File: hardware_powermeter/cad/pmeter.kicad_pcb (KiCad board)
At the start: 4 copper layers, 47 x 14 mm, 59 parts, among them J101 conector magnetico 6 vias, J102 furos da celula, J301 furos da ponte, U101 nPM1100-QDAB, U102 MAX17048G+T10, U201 HOLYIOT-26001-A, U301 ADS1220IRVAR, U302 TPS22916BYFPR, U401 BMA400, U402 TMP117AIDRVR

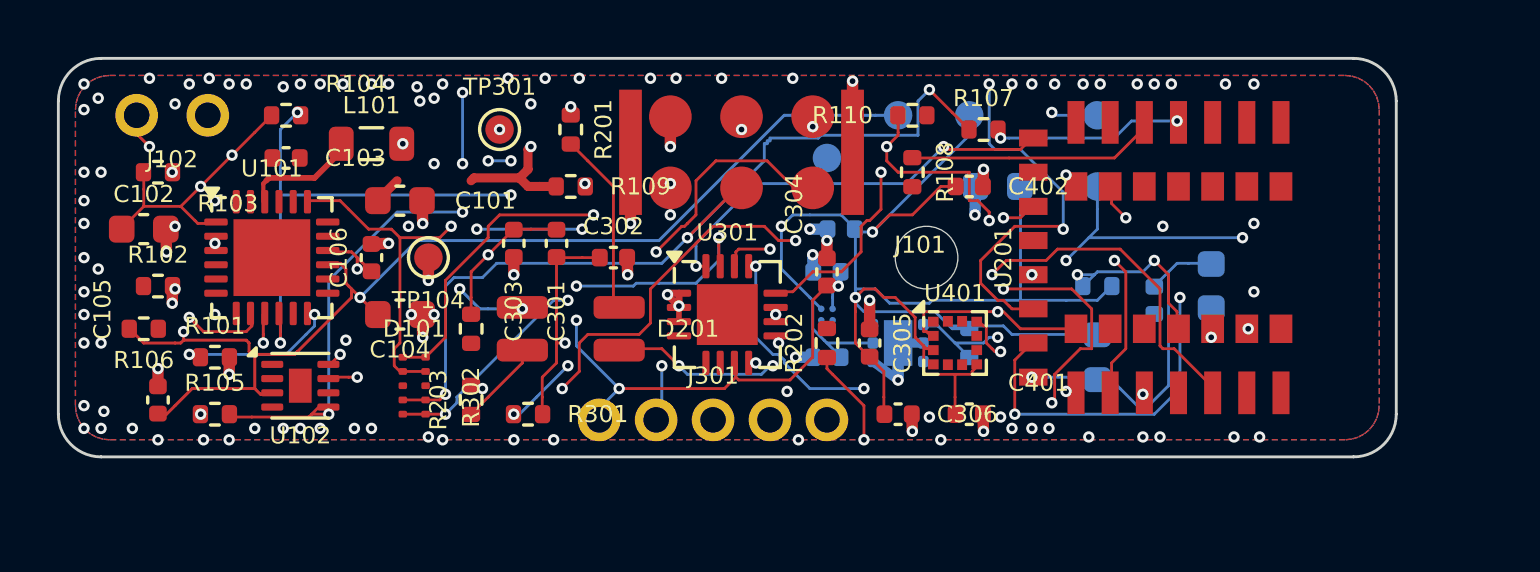
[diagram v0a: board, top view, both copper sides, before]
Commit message: feat(hardware): move the cell beside the board and put every passive on the back
The owner's decision on 2026-09-30, and it changes the board more than it
changes the pod. The cell used to lie against the back over x 1.5 to 26 -
the whole energy block - so the parts that needed relief the most had no
back face at all. Beside the board it takes nothing, the back is free end
to end, and the pod loses the cell from its stack: about 6.5 mm tall
instead of 10.

So the board is 50 x 16 (it grows more across than along, which is the pod
shape that is wanted: low and wide, not long), the back ceiling is 1.5 mm,
and 43 of the 58 parts move to it - every resistor, every capacitor and the
ferrite. Only C104 and C105 stay on the front, because the buck's switching
loop must not cross the board.

The reason is measured, not argued. On the empty grid, before a single
track: F.Cu had 55.2% of its cells free, In2.Cu 87.1% and B.Cu 81.6%.
Nearly half the top layer was pad and clearance, and every routing failure
read "sem caminho ate (x; y) na camada 0". Thinning the track does not fix
that, because the pad does not thin.

What it bought, all from the dry run and the DRC:

  AL1  11 of 19 capacitors out of limit, 3.85 mm average -> 5 of 19, 1.59
  AN1  the analogue corner 3.3 mm from the buck -> 10.9 mm, and 5.9 from
       the module: MET
  AN2  filter parts up to 9.8 mm from their pin -> 3.8 mm at most: MET
  US1  serial over the switching node: MET
  dry run 14 rules met and 6 violated -> 18 met and 2 violated
  routing 93 connections -> 99, and still zero DRC errors

A decoupling capacitor on the back, under the pin it serves, is one via
away - closer than anything that was left free on the front, which is what
AL1 had been asking for all along.

Track and clearance are the fabricator's minimum for four layers (0.0889),
with the router drawing 0.09 and keeping its own clearance at 0.10. That
last number is not cosmetic: at 0.09 the project's own check became LOOSER
than the DRC 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
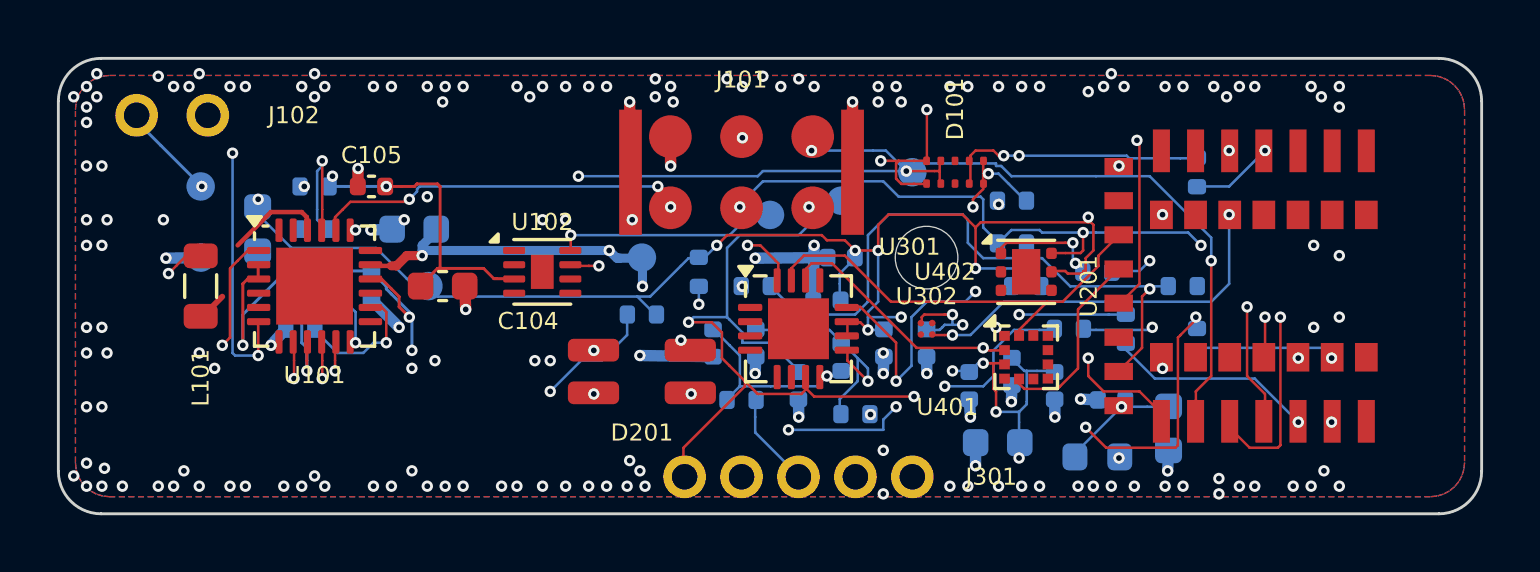
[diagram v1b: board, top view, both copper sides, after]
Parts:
- C101, C102, C103, C106, C301, C302, C303, C304, C305, C306, C401, C402, R101, R102, R103, R104, R105, R106, R107, R108, R109, R110, R201, R202, R203, R301, R302, TP104, TP301: moved to B.Cu
- U302, U402: moved to F.Cu
- moved R105 28.9 mm to (59.0, 33.0)
- moved TP102 24.6 mm to (30.0, 29.5)
- moved R201 23.2 mm to (65.0, 35.0)
- moved R203 23.1 mm to (62.5, 34.5)
- moved D101 20.4 mm to (56.5, 29.0), turned to 90 degrees
- moved TP103 19.9 mm to (38.0, 33.0)
- moved R103 17.7 mm to (45.5, 34.0)
- moved R104 15.5 mm to (47.5, 32.5), turned to 90 degrees
- moved TP301 12.3 mm to (52.5, 30.0)
- moved TP201 11.5 mm to (50.0, 30.5)
- moved R301 11.5 mm to (53.0, 37.5)
- moved R110 11.2 mm to (64.5, 33.0), turned to 180 degrees
- moved C301 10.8 mm to (52.5, 35.5)
- moved C105 10.6 mm to (36.0, 29.5), turned to 180 degrees
- moved R302 9.82 mm to (49.0, 37.0), turned to 0 degrees
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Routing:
- net SHPACT: track 0.00 -> 55.5 mm, vias 0 -> 3
- net GAUGE_ALRT: track 50.8 -> 0.00 mm, vias 6 -> 0
- net VBAT: track 48.2 -> 19.1 mm
- net LED_B: track 35.3 -> 7.34 mm, vias 4 -> 1
- net LED_R: track 31.0 -> 5.07 mm, vias 2 -> 1
- net 3V0: track 109.3 -> 85.1 mm, vias 10 -> 16
- net LED_KG: track 34.2 -> 14.2 mm, vias 5 -> 2
- net LED_KR: track 6.50 -> 26.0 mm, vias 0 -> 3
- net LED_KB: track 3.05 -> 22.2 mm, vias 0 -> 4
- net VBUS_SENSE: track 38.9 -> 22.1 mm, vias 5 -> 1
- net IMU_CS: track 16.6 -> 0.00 mm, vias 2 -> 0
- net EXC_EN: track 0.00 -> 13.6 mm, vias 0 -> 2
- net ERR_N: track 38.3 -> 51.0 mm, vias 4 -> 3
- net UART_RX: track 57.8 -> 46.1 mm, vias 4 -> 5
- net LED_G: track 0.00 -> 11.4 mm, vias 0 -> 2
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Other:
- board size 47 x 14 mm -> 50 x 16 mm
- board text added: "BIKE POWER METER - placa 50 x 16 mm, 0.8 mm, 4 camadas"
- board text removed: "BIKE POWER METER - placa 47 x 14 mm, 0.8 mm, 4 camadas"

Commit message: feat(hardware): the routed board, its drawings and the pod that no longer fits
663 tracks, 172 vias, ZERO DRC errors and 17 connections still open, on the
50 x 16 board with every passive on the back. The seven copper sheets, the
assembly drawing, the 3D views and the pod's STLs were all regenerated from
it.

The pod now FAILS its own PD10 and PD17, and that is correct: it is 21.0 mm
wide against the 20 mm target, because the board grew to 16 mm while the pod
still stacks the cell UNDER it (floor 1.0 + cell 4.0 + air 0.5 + board 0.8 +
ceiling 2.7 + lid 1.0). The decision of 2026-09-30 was to put the cell BESIDE
the board so the device gets lower; the board was rebuilt for it and the pod
was not. The dry run says so out loud instead of hiding it, which is what it
is for.
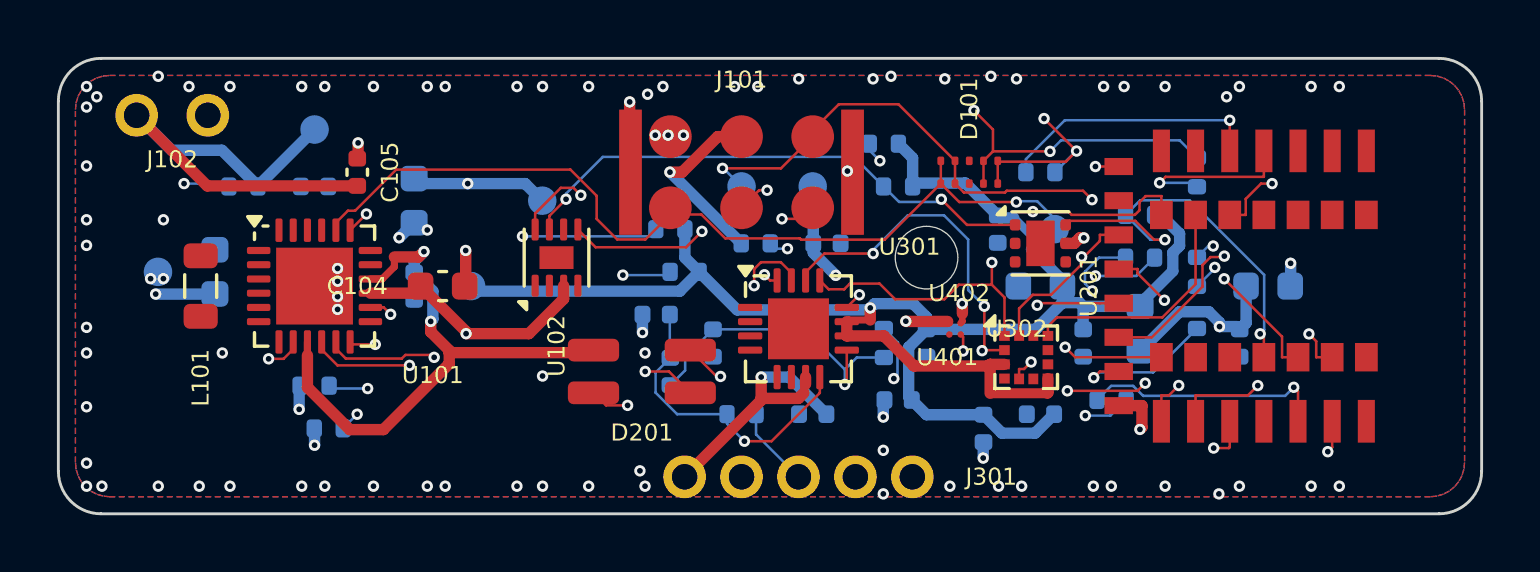
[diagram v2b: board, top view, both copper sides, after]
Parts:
- moved TP201 10.0 mm to (60.0, 31.0)
- moved R205 7.62 mm to (54.5, 29.5)
- moved R105 7.07 mm to (54.0, 28.0)
- moved C202 6.10 mm to (67.5, 33.0), turned to 180 degrees
- moved C301 6.02 mm to (46.5, 36.0), turned to -90 degrees
- moved TP202 6.02 mm to (49.0, 29.5)
- moved C203 5.70 mm to (59.5, 33.0)
- moved C308 5.59 mm to (58.0, 31.0), turned to 90 degrees
- moved C307 4.95 mm to (52.0, 31.5), turned to 180 degrees
- moved C201 4.92 mm to (66.5, 35.0), turned to 90 degrees
- moved FB201 4.74 mm to (63.0, 34.5), turned to 90 degrees
- moved R204 4.61 mm to (63.0, 30.5)
- moved TP102 4.47 mm to (34.0, 27.5)
- moved C305 4.30 mm to (54.5, 37.0)
- moved TP101 4.03 mm to (42.0, 30.0)
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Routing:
- net SHPACT: track 55.5 -> 0.00 mm, vias 3 -> 0
- net GAUGE_ALRT: track 0.00 -> 32.9 mm, vias 0 -> 3
- net VBAT: track 19.1 -> 40.3 mm, vias 3 -> 1
- net I2C_SDA: track 33.4 -> 50.8 mm, vias 4 -> 3
- net SPI_MISO: track 8.14 -> 24.5 mm
- net SHPHLD: track 8.10 -> 22.5 mm
- net EXC_EN: track 13.6 -> 27.7 mm, vias 2 -> 4
- net GND: track 24.9 -> 11.2 mm, vias 165 -> 91
- net 3V0: track 85.1 -> 71.6 mm, vias 16 -> 3
- net VBUS_SENSE: track 22.1 -> 35.5 mm, vias 1 -> 2
- net 3V0_EXC: track 33.5 -> 22.2 mm, vias 4 -> 3
- net SPI_SCK: track 15.6 -> 25.5 mm, vias 0 -> 2
- net ERR_N: track 51.0 -> 41.1 mm
- net LED_G: track 11.4 -> 21.1 mm
- net SWCLK_J: track 9.56 -> 18.3 mm
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
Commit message: feat(hardware): net classes from the current table, and the ground left to its plane
Two changes to what the DSN tells Freerouting, both because the router can
only be as good as what it is told.

The three hand-written net classes lied in both directions. Measured against
the IPC-2221 width that route.largura() computes for each net:

    net         IPC asks   the DSN sent
    3V0            0.090       0.40
    3V0_EXC        0.090       0.40
    3V0_MOD        0.090       0.40
    VBAT           0.105       0.40
    VSYS           0.105       0.40
    BUCK_SW        0.204       0.09

Four times wider than the norm asks spends channel that is needed - 3V0 was
one of the nets that would not close - and BUCK_SW, which carries the
inductor's 350 mA, went at signal width. make_netclasses.py now generates one
class per width, rounded up in steps of 0.01 mm, straight from that table.
AL2 passes with ZERO narrowings as a result.

The USB class is gone with them: the nRF54L15 has no USB, the two contacts
that carried D+ and D- now carry UART, and there is no differential pair on
this board. An unused differential-pair class was what gave Freerouting a
narrower width to fall back on - ten tracks of 0.0674 mm.

And GND leaves the DSN entirely. It is 51 of this board's 159 connections,
32 percent, and every one of them is answered by the pour of its own face
plus a stitching via, which stitch_gnd.py places afterwards. Letting the
router spend a third of its space on what the plane already solves is waste.

What was tried and measured as NOT worth it, so it is not here: a 0.45 mm
escape ring around all seven fine-pitch ICs closed one more connection (16
against 17) and took AL1 from 11 to 12 capacitors out of limit, with C105
15.6 mm from the U102 it decouples - at that distance it decouples nothing.
The ring on U101 alone gave 18, worse than no ring. All three sit inside the
router's own run-to-run variation, so what decides is the number that does
not vary: how far the dec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
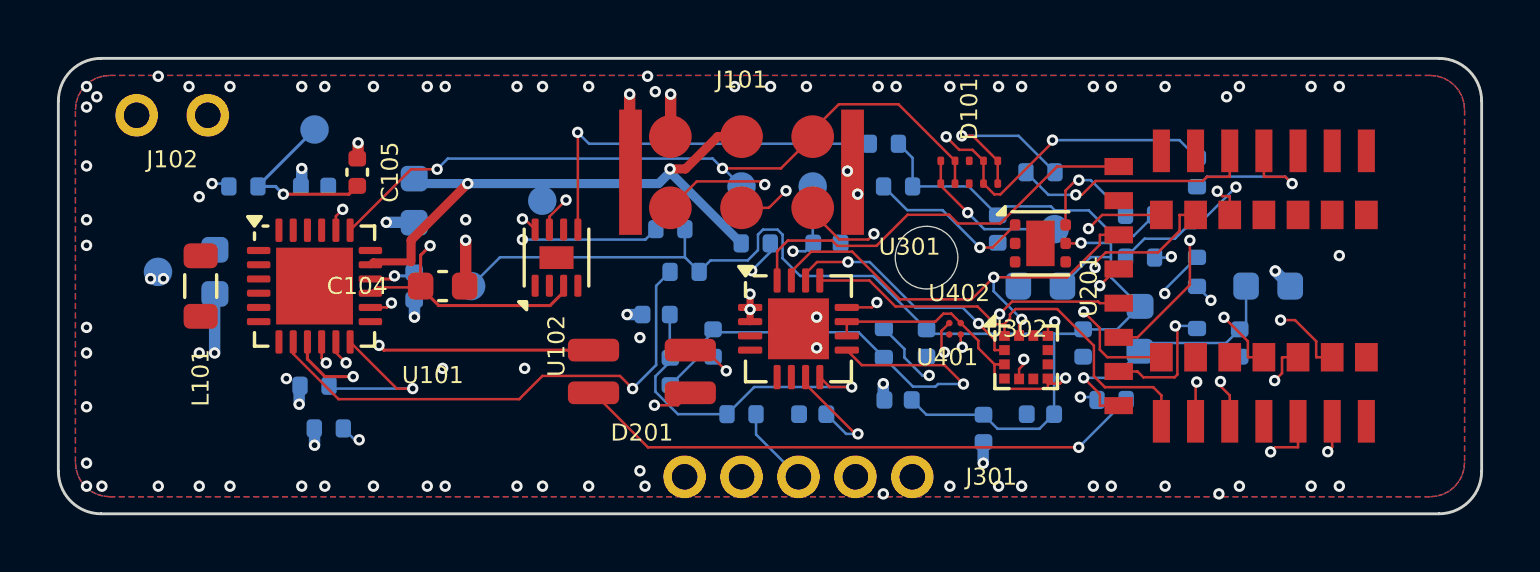
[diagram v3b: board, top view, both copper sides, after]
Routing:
- net LED_KG: track 22.5 -> 39.5 mm
- net I2C_SDA: track 50.8 -> 36.0 mm
- net VBAT: track 40.3 -> 27.9 mm, vias 1 -> 2
- net SHPHLD: track 22.5 -> 13.1 mm
- net GAUGE_ALRT: track 32.9 -> 42.3 mm, vias 3 -> 2
- net SPI_SCK: track 25.5 -> 16.4 mm
- net UART_TX: track 47.1 -> 55.6 mm, vias 2 -> 4
- net SPI_MISO: track 24.5 -> 16.1 mm, vias 2 -> 0
- net UART_RX: track 43.7 -> 51.2 mm, vias 4 -> 3
- net I2C_SCL: track 34.6 -> 41.1 mm
- net LED_KR: track 26.1 -> 32.6 mm
- net AIN_P: track 11.1 -> 16.8 mm
- net 3V0: track 71.6 -> 66.3 mm, vias 3 -> 2
- net SWCLK_J: track 18.3 -> 13.7 mm, vias 3 -> 2
- net VSYS: track 20.4 -> 15.8 mm, vias 2 -> 3
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
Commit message: feat(hardware): give the router a bare board - the pour comes after the track
The owner's rule, and it is the right order: first the copper that carries
signal, then the ground around it.

KiCad exports each pour as (plane GND (polygon <layer> ...)), and there are
three: In1.Cu, which is the real plane, and F.Cu and B.Cu, which are the
faces Freerouting draws on. On those two the pour is only in the way - it is
already there, covering everything, before a single track exists, and
Freerouting's own v2.4.1 notes warn that routing over a copper plane produces
clearance violations. It was drawing one of them that crashed its renderer.

So the two routing-face pours leave the DSN, and fill_zones.py pours them
back afterwards, around the copper that ended up there. The inner plane
stays, because nothing is routed on it.

Measured: 16 connections open against 20, with Freerouting down to 9 it could
not route, and still zero DRC errors on 661 tracks and 182 vias.
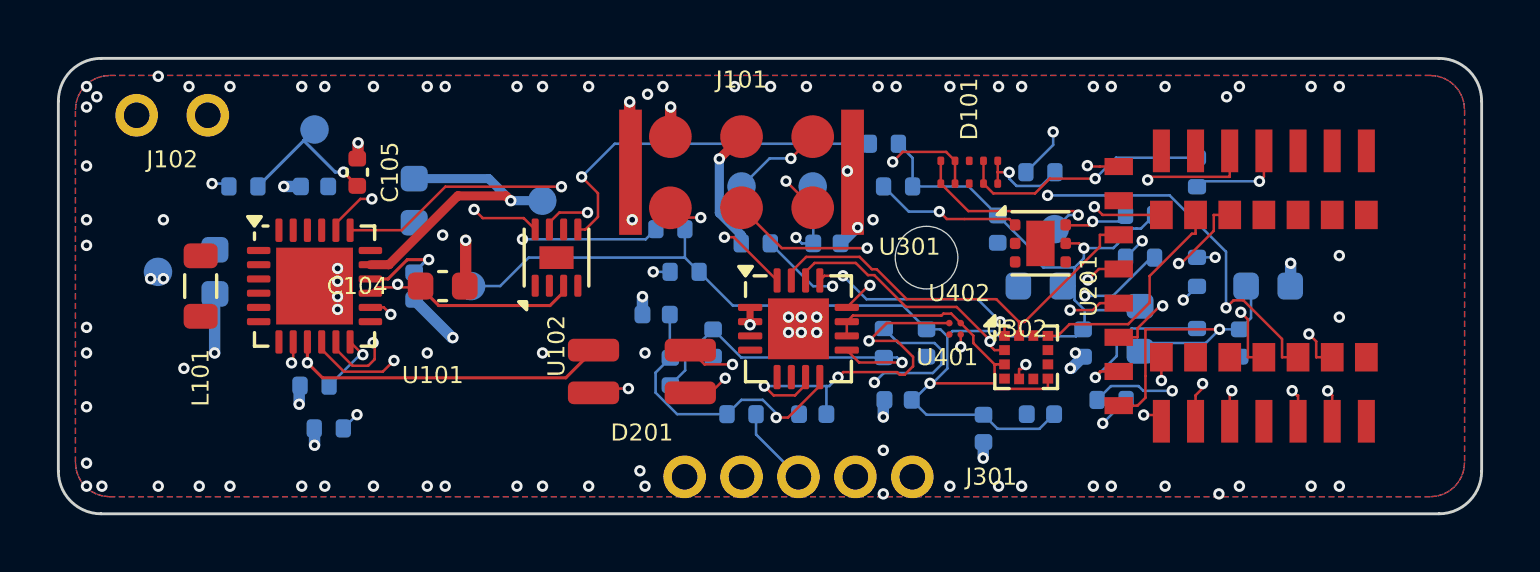
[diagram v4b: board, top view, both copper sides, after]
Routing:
- net LED_KG: track 39.5 -> 18.9 mm
- net VBUS_SENSE: track 32.9 -> 22.7 mm
- net LED_KR: track 32.6 -> 42.4 mm
- net AIN_P: track 16.8 -> 11.8 mm
- net LED_G: track 16.7 -> 11.9 mm
- net VSYS: track 15.8 -> 20.4 mm, vias 3 -> 2
- net I2C_SDA: track 36.0 -> 40.5 mm
- net SHPHLD: track 13.1 -> 17.2 mm
- net ICHG: track 5.86 -> 2.27 mm
- net SWDIO_J: track 19.4 -> 23.0 mm, vias 3 -> 2
- net 3V0: track 66.3 -> 63.1 mm
- net ADC_CS: track 14.7 -> 17.4 mm, vias 0 -> 2
- net SWDIO: track 5.60 -> 3.41 mm
- net VBAT: track 27.9 -> 25.9 mm
- net 3V0_MOD: track 9.68 -> 11.6 mm
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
